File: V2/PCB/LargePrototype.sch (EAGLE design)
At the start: 205 parts, among them U1 GENERIC-SOIC8, U2 GENERIC-SOIC8, U3 GENERIC-SOIC8, U4 GENERIC-SOIC8

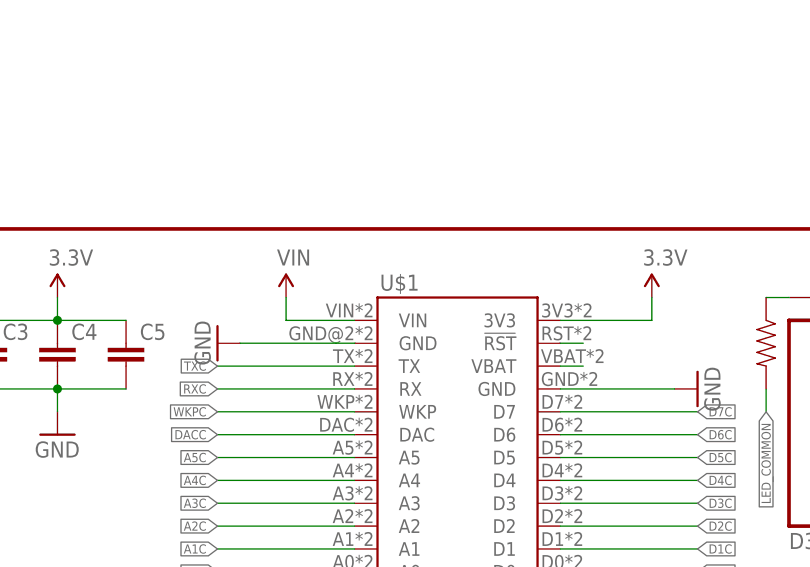
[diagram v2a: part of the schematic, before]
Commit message: Renamed electron & added pictures.
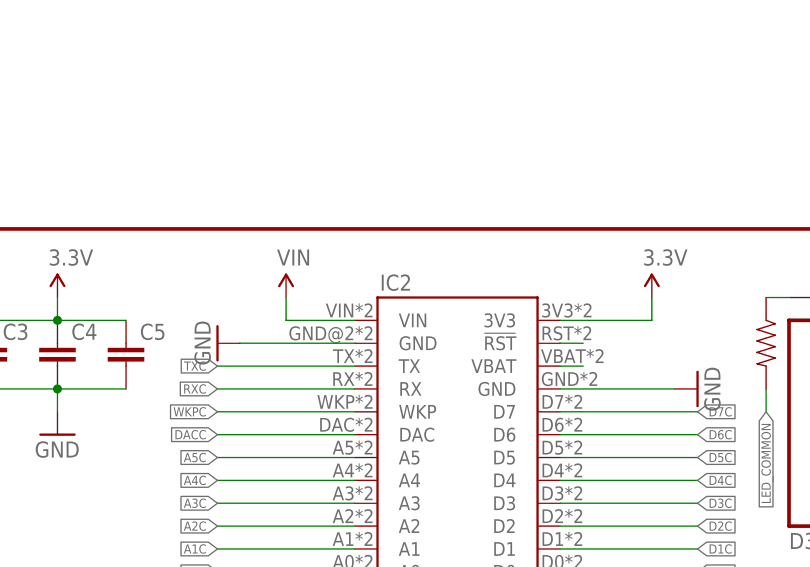
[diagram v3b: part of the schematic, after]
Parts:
- renumbered U$1 to IC2
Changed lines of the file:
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@@
 </classes>
 <parts>
-<part name="U$1" library="Tinamous" deviceset="ELECTRON" device="DUALNAMED"/>
+<part name="IC2" library="Tinamous" deviceset="ELECTRON" device="DUALNAMED"/>
 <part name="FRAME1" library="SparkFun-Aesthetics" deviceset="FRAME-LETTER" device=""/>
 <part name="IC1" library="v-reg" deviceset="78XXS" device=""/>
@@
 </plain>
 <instances>
-<instance part="U$1" gate="G$1" x="111.76" y="154.94"/>
+<instance part="IC2" gate="G$1" x="111.76" y="154.94"/>
 <instance part="FRAME1" gate="G$1" x="0" y="0"/>
 <instance part="FRAME1" gate="V" x="147.32" y="0"/>
@@
 </segment>
 <segment>
-<pinref part="U$1" gate="G$1" pin="3V3"/>
+<pinref part="IC2" gate="G$1" pin="3V3"/>
 <pinref part="SUPPLY2" gate="G$1" pin="3.3V"/>
 <wire x1="124.46" y1="175.26" x2="134.62" y2="175.26" width="0.1524" layer="91"/>
@@
 </segment>
 <segment>
-<pinref part="U$1" gate="G$1" pin="GND@2"/>
+<pinref part="IC2" gate="G$1" pin="GND@2"/>
 <pinref part="GND5" gate="1" pin="GND"/>
 <wire x1="101.6" y1="172.72" x2="88.9" y2="172.72" width="0.1524" layer="91"/>
 </segment>
 <segment>
-<pinref part="U$1" gate="G$1" pin="GND"/>
+<pinref part="IC2" gate="G$1" pin="GND"/>
 <pinref part="GND2" gate="1" pin="GND"/>
 <wire x1="124.46" y1="167.64" x2="137.16" y2="167.64" width="0.1524" layer="91"/>
@@
 </segment>
 <segment>
-<pinref part="U$1" gate="G$1" pin="VIN"/>
+<pinref part="IC2" gate="G$1" pin="VIN"/>
 <pinref part="SUPPLY3" gate="G$1" pin="VIN"/>
 <wire x1="101.6" y1="175.26" x2="93.98" y2="175.26" width="0.1524" layer="91"/>
@@
 <net name="N$110" class="0">
 <segment>
-<pinref part="U$1" gate="G$1" pin="VBAT"/>
+<pinref part="IC2" gate="G$1" pin="VBAT"/>
 <wire x1="124.46" y1="170.18" x2="127" y2="170.18" width="0.1524" layer="91"/>
 </segment>
@@
 <net name="N$111" class="0">
 <segment>
-<pinref part="U$1" gate="G$1" pin="!RST"/>
+<pinref part="IC2" gate="G$1" pin="!RST"/>
 <wire x1="124.46" y1="172.72" x2="127" y2="172.72" width="0.1524" layer="91"/>
 </segment>
@@
 <segment>
 <label x="86.36" y="132.08" size="1.016" layer="95" rot="R180" xref="yes"/>
-<pinref part="U$1" gate="G$1" pin="B0"/>
+<pinref part="IC2" gate="G$1" pin="B0"/>
 <wire x1="86.36" y1="132.08" x2="101.6" y2="132.08" width="0.1524" layer="91"/>
 </segment>
@@
 <segment>
 <label x="86.36" y="134.62" size="1.016" layer="95" rot="R180" xref="yes"/>
-<pinref part="U$1" gate="G$1" pin="B1"/>
+<pinref part="IC2" gate="G$1" pin="B1"/>
 <wire x1="101.6" y1="134.62" x2="86.36" y2="134.62" width="0.1524" layer="91"/>
 </segment>
@@
 <segment>
 <label x="86.36" y="137.16" size="1.016" layer="95" rot="R180" xref="yes"/>
-<pinref part="U$1" gate="G$1" pin="B2"/>
+<pinref part="IC2" gate="G$1" pin="B2"/>
 <wire x1="101.6" y1="137.16" x2="86.36" y2="137.16" width="0.1524" layer="91"/>
 </segment>
@@
 <segment>
 <label x="86.36" y="139.7" size="1.016" layer="95" rot="R180" xref="yes"/>
-<pinref part="U$1" gate="G$1" pin="B3"/>
+<pinref part="IC2" gate="G$1" pin="B3"/>
 <wire x1="86.36" y1="139.7" x2="101.6" y2="139.7" width="0.1524" layer="91"/>
 </segment>
@@
 <segment>
 <label x="86.36" y="142.24" size="1.016" layer="95" rot="R180" xref="yes"/>
-<pinref part="U$1" gate="G$1" pin="B4"/>
+<pinref part="IC2" gate="G$1" pin="B4"/>
 <wire x1="101.6" y1="142.24" x2="86.36" y2="142.24" width="0.1524" layer="91"/>
 </segment>
@@
 <segment>
 <label x="86.36" y="144.78" size="1.016" layer="95" rot="R180" xref="yes"/>
-<pinref part="U$1" gate="G$1" pin="B5"/>
+<pinref part="IC2" gate="G$1" pin="B5"/>
 <wire x1="86.36" y1="144.78" x2="101.6" y2="144.78" width="0.1524" layer="91"/>
 </segment>
@@
 <segment>
 <label x="86.36" y="147.32" size="1.016" layer="95" rot="R180" xref="yes"/>
-<pinref part="U$1" gate="G$1" pin="A0"/>
+<pinref part="IC2" gate="G$1" pin="A0"/>
 <wire x1="101.6" y1="147.32" x2="86.36" y2="147.32" width="0.1524" layer="91"/>
 </segment>
@@
 <segment>
 <label x="86.36" y="149.86" size="1.016" layer="95" rot="R180" xref="yes"/>
-<pinref part="U$1" gate="G$1" pin="A1"/>
+<pinref part="IC2" gate="G$1" pin="A1"/>
 <wire x1="86.36" y1="149.86" x2="101.6" y2="149.86" width="0.1524" layer="91"/>
 </segment>
@@
 <segment>
 <label x="86.36" y="152.4" size="1.016" layer="95" rot="R180" xref="yes"/>
-<pinref part="U$1" gate="G$1" pin="A2"/>
+<pinref part="IC2" gate="G$1" pin="A2"/>
 <wire x1="101.6" y1="152.4" x2="86.36" y2="152.4" width="0.1524" layer="91"/>
 </segment>
@@
 <segment>
 <label x="86.36" y="154.94" size="1.016" layer="95" rot="R180" xref="yes"/>
-<pinref part="U$1" gate="G$1" pin="A3"/>
+<pinref part="IC2" gate="G$1" pin="A3"/>
 <wire x1="86.36" y1="154.94" x2="101.6" y2="154.94" width="0.1524" layer="91"/>
 </segment>
@@
 <segment>
 <label x="86.36" y="157.48" size="1.016" layer="95" rot="R180" xref="yes"/>
-<pinref part="U$1" gate="G$1" pin="A4"/>
+<pinref part="IC2" gate="G$1" pin="A4"/>
 <wire x1="101.6" y1="157.48" x2="86.36" y2="157.48" width="0.1524" layer="91"/>
 </segment>
@@
 <segment>
 <label x="86.36" y="160.02" size="1.016" layer="95" rot="R180" xref="yes"/>
-<pinref part="U$1" gate="G$1" pin="A5"/>
+<pinref part="IC2" gate="G$1" pin="A5"/>
 <wire x1="86.36" y1="160.02" x2="101.6" y2="160.02" width="0.1524" layer="91"/>
 </segment>
@@
 <segment>
 <label x="86.36" y="162.56" size="1.016" layer="95" rot="R180" xref="yes"/>
-<pinref part="U$1" gate="G$1" pin="DAC"/>
+<pinref part="IC2" gate="G$1" pin="DAC"/>
 <wire x1="86.36" y1="162.56" x2="101.6" y2="162.56" width="0.1524" layer="91"/>
 </segment>
@@
 <segment>
 <label x="86.36" y="165.1" size="1.016" layer="95" rot="R180" xref="yes"/>
-<pinref part="U$1" gate="G$1" pin="WKP"/>
+<pinref part="IC2" gate="G$1" pin="WKP"/>
 <wire x1="86.36" y1="165.1" x2="101.6" y2="165.1" width="0.1524" layer="91"/>
 </segment>
@@
 <segment>
 <label x="86.36" y="167.64" size="1.016" layer="95" rot="R180" xref="yes"/>
-<pinref part="U$1" gate="G$1" pin="RX"/>
+<pinref part="IC2" gate="G$1" pin="RX"/>
 <wire x1="86.36" y1="167.64" x2="101.6" y2="167.64" width="0.1524" layer="91"/>
 </segment>
@@
 <segment>
 <label x="86.36" y="170.18" size="1.016" layer="95" rot="R180" xref="yes"/>
-<pinref part="U$1" gate="G$1" pin="TX"/>
+<pinref part="IC2" gate="G$1" pin="TX"/>
 <wire x1="101.6" y1="170.18" x2="86.36" y2="170.18" width="0.1524" layer="91"/>
 </segment>
@@
 <segment>
 <label x="139.7" y="132.08" size="1.016" layer="95" xref="yes"/>
-<pinref part="U$1" gate="G$1" pin="C0"/>
+<pinref part="IC2" gate="G$1" pin="C0"/>
 <wire x1="139.7" y1="132.08" x2="124.46" y2="132.08" width="0.1524" layer="91"/>
 </segment>
@@
 <segment>
 <label x="139.7" y="134.62" size="1.016" layer="95" xref="yes"/>
-<pinref part="U$1" gate="G$1" pin="C1"/>
+<pinref part="IC2" gate="G$1" pin="C1"/>
 <wire x1="139.7" y1="134.62" x2="124.46" y2="134.62" width="0.1524" layer="91"/>
 </segment>
@@
 <segment>
 <label x="139.7" y="137.16" size="1.016" layer="95" xref="yes"/>
-<pinref part="U$1" gate="G$1" pin="C2"/>
+<pinref part="IC2" gate="G$1" pin="C2"/>
 <wire x1="139.7" y1="137.16" x2="124.46" y2="137.16" width="0.1524" layer="91"/>
 </segment>
@@
 <segment>
 <label x="139.7" y="139.7" size="1.016" layer="95" xref="yes"/>
-<pinref part="U$1" gate="G$1" pin="C3"/>
+<pinref part="IC2" gate="G$1" pin="C3"/>
 <wire x1="139.7" y1="139.7" x2="124.46" y2="139.7" width="0.1524" layer="91"/>
 </segment>
@@
 <segment>
 <label x="139.7" y="142.24" size="1.016" layer="95" xref="yes"/>
-<pinref part="U$1" gate="G$1" pin="C4"/>
+<pinref part="IC2" gate="G$1" pin="C4"/>
 <wire x1="139.7" y1="142.24" x2="124.46" y2="142.24" width="0.1524" layer="91"/>
 </segment>
@@
 <segment>
 <label x="139.7" y="144.78" size="1.016" layer="95" xref="yes"/>
-<pinref part="U$1" gate="G$1" pin="C5"/>
+<pinref part="IC2" gate="G$1" pin="C5"/>
 <wire x1="139.7" y1="144.78" x2="124.46" y2="144.78" width="0.1524" layer="91"/>
 </segment>
@@
 <segment>
 <label x="139.7" y="147.32" size="1.016" layer="95" xref="yes"/>
-<pinref part="U$1" gate="G$1" pin="D0"/>
+<pinref part="IC2" gate="G$1" pin="D0"/>
 <wire x1="139.7" y1="147.32" x2="124.46" y2="147.32" width="0.1524" layer="91"/>
 </segment>
@@
 <segment>
 <label x="139.7" y="149.86" size="1.016" layer="95" xref="yes"/>
-<pinref part="U$1" gate="G$1" pin="D1"/>
+<pinref part="IC2" gate="G$1" pin="D1"/>
 <wire x1="139.7" y1="149.86" x2="124.46" y2="149.86" width="0.1524" layer="91"/>
 </segment>
@@
 <segment>
 <label x="139.7" y="152.4" size="1.016" layer="95" xref="yes"/>
-<pinref part="U$1" gate="G$1" pin="D2"/>
+<pinref part="IC2" gate="G$1" pin="D2"/>
 <wire x1="139.7" y1="152.4" x2="124.46" y2="152.4" width="0.1524" layer="91"/>
 </segment>
@@
 <segment>
 <label x="139.7" y="154.94" size="1.016" layer="95" xref="yes"/>
-<pinref part="U$1" gate="G$1" pin="D3"/>
+<pinref part="IC2" gate="G$1" pin="D3"/>
 <wire x1="139.7" y1="154.94" x2="124.46" y2="154.94" width="0.1524" layer="91"/>
 </segment>
@@
 <segment>
 <label x="139.7" y="157.48" size="1.016" layer="95" xref="yes"/>
-<pinref part="U$1" gate="G$1" pin="D4"/>
+<pinref part="IC2" gate="G$1" pin="D4"/>
 <wire x1="139.7" y1="157.48" x2="124.46" y2="157.48" width="0.1524" layer="91"/>
 </segment>
@@
 <segment>
 <label x="139.7" y="160.02" size="1.016" layer="95" xref="yes"/>
-<pinref part="U$1" gate="G$1" pin="D5"/>
+<pinref part="IC2" gate="G$1" pin="D5"/>
 <wire x1="139.7" y1="160.02" x2="124.46" y2="160.02" width="0.1524" layer="91"/>
 </segment>
@@
 <segment>
 <label x="139.7" y="162.56" size="1.016" layer="95" xref="yes"/>
-<pinref part="U$1" gate="G$1" pin="D6"/>
+<pinref part="IC2" gate="G$1" pin="D6"/>
 <wire x1="139.7" y1="162.56" x2="124.46" y2="162.56" width="0.1524" layer="91"/>
 </segment>
@@
 <segment>
 <label x="139.7" y="165.1" size="1.016" layer="95" xref="yes"/>
-<pinref part="U$1" gate="G$1" pin="D7"/>
+<pinref part="IC2" gate="G$1" pin="D7"/>
 <wire x1="139.7" y1="165.1" x2="124.46" y2="165.1" width="0.1524" layer="91"/>
 </segment>
